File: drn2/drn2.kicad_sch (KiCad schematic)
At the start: 55 parts, among them J1 Conn_01x03_Socket, J10 Conn_01x03_Socket, J11 Conn_01x03_Socket, J12 Conn_01x03_Socket, J13 Conn_01x03_Socket, J14GND Conn_01x03_Socket, J15GND Conn_01x03_Socket, J16 Conn_01x03_Socket, J2 Raspberry_Pi_2_3, J3 Conn_01x03_Socket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

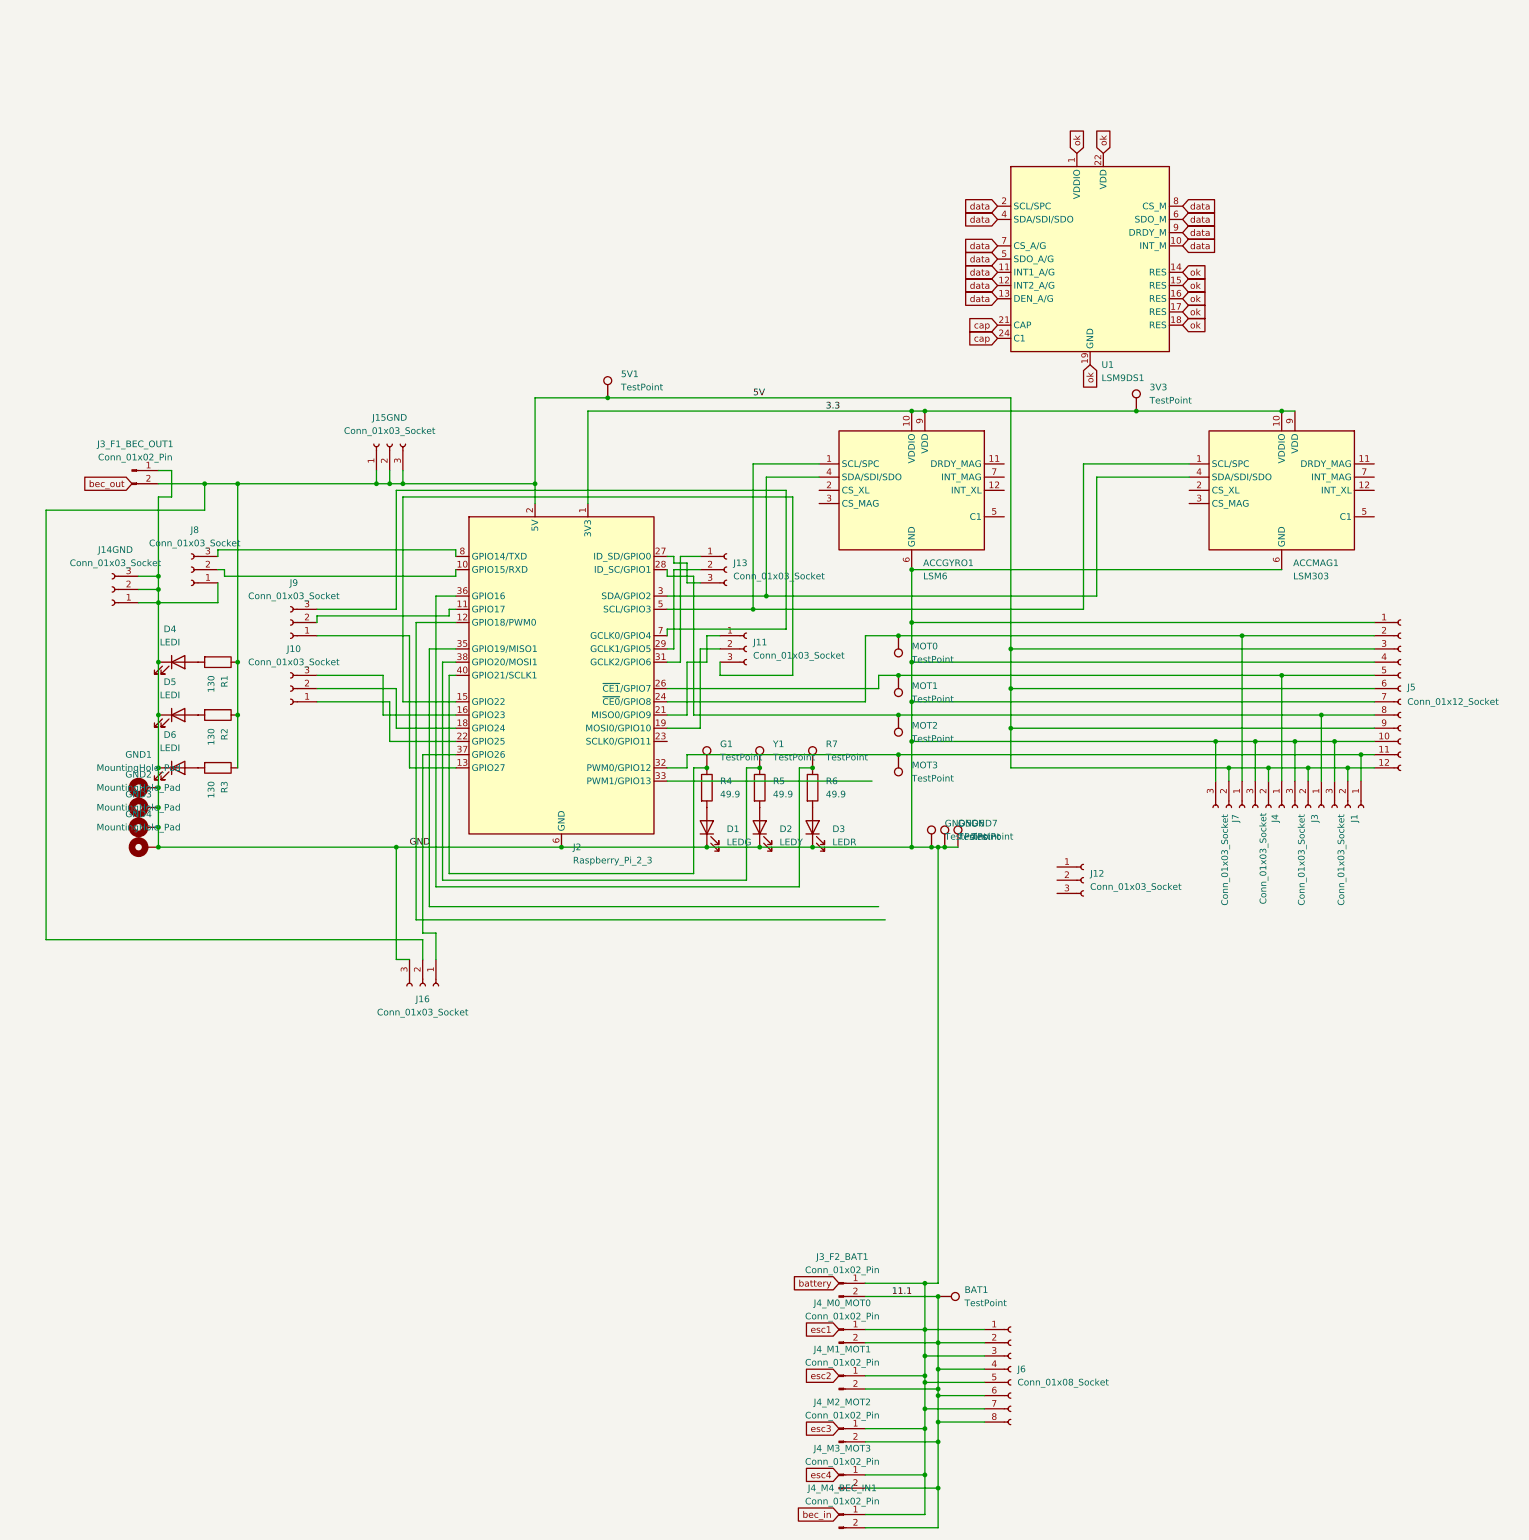
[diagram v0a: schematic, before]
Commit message: feat: pcb version 2.8
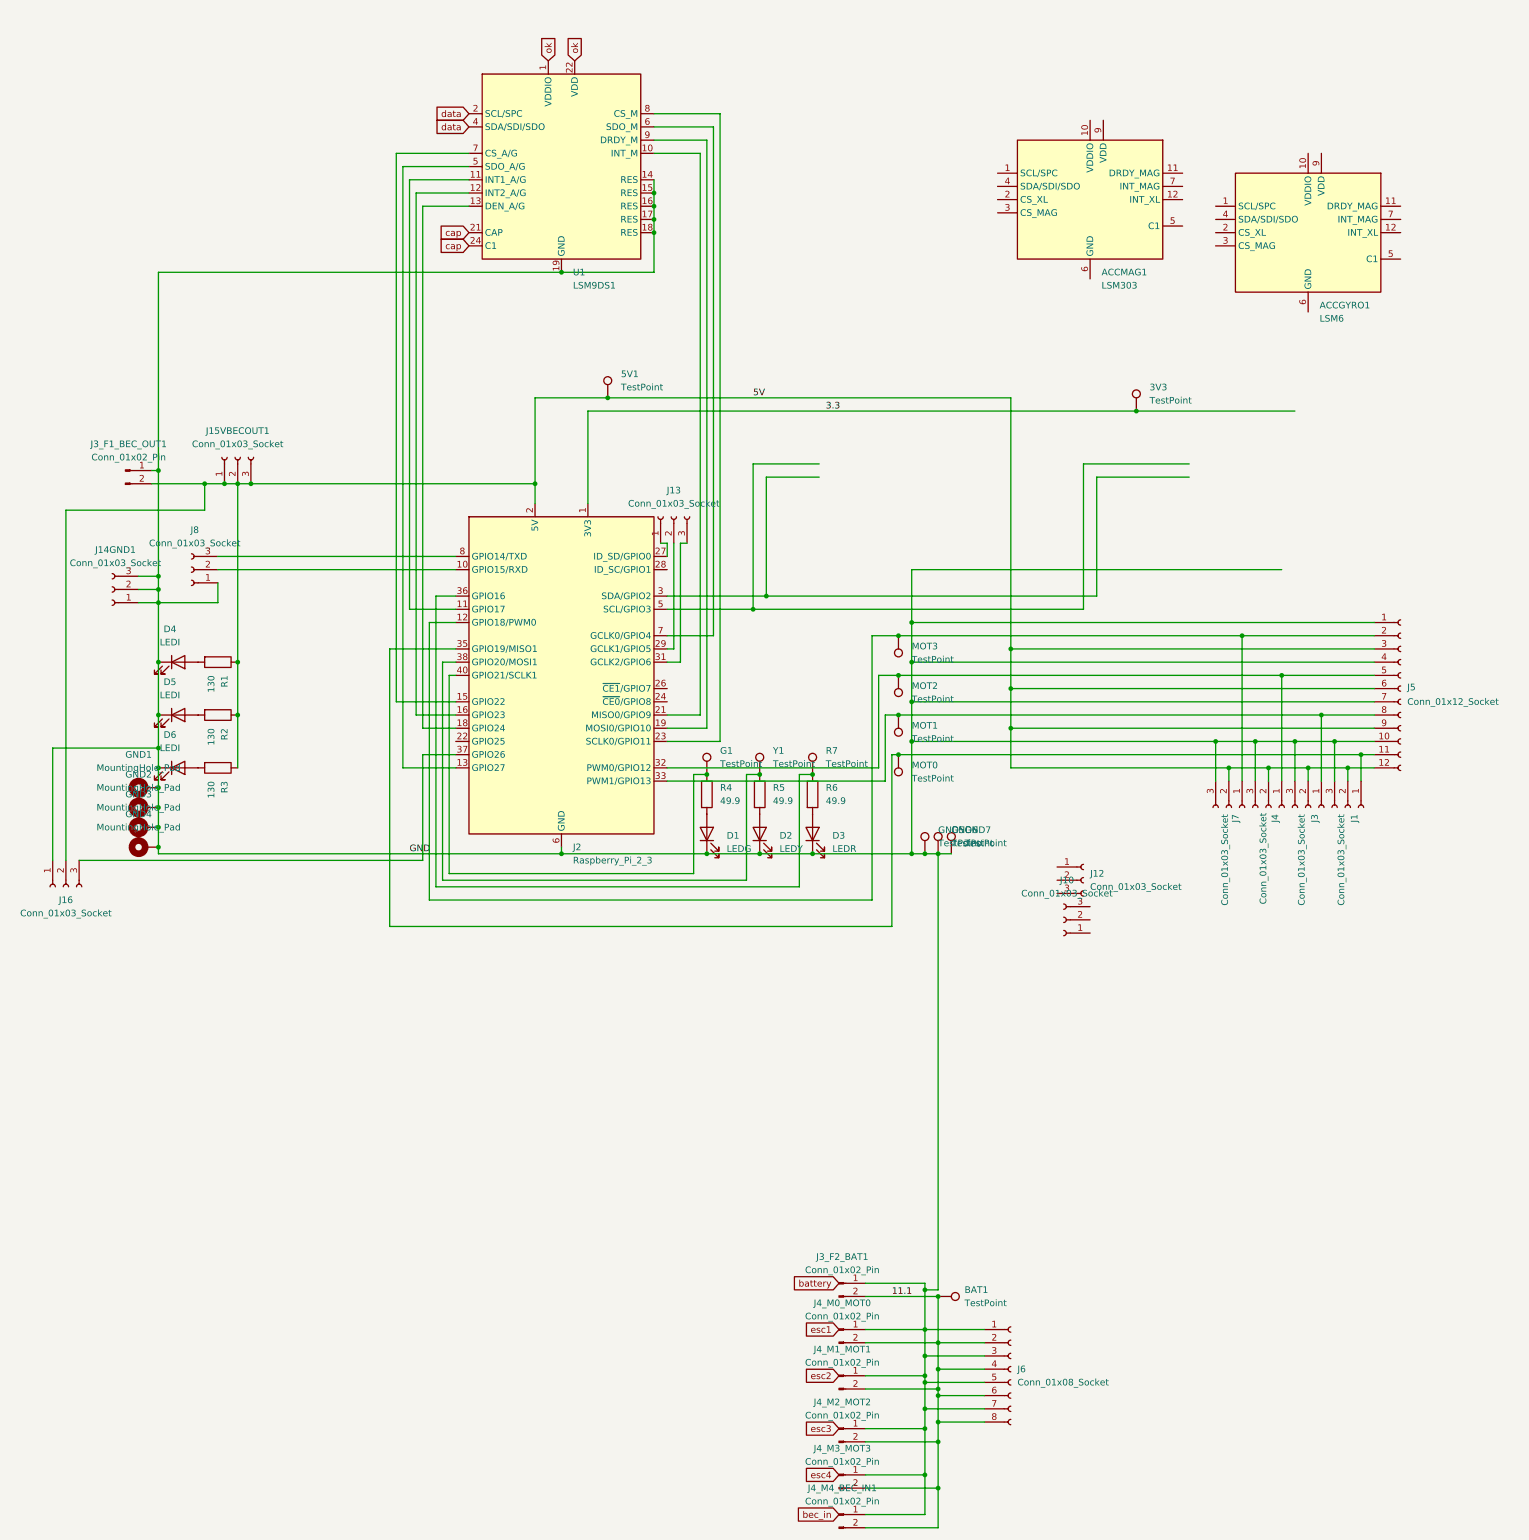
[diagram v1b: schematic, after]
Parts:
- removed J11, J9: Conn_01x03_Socket, Connector_PinHeader_2.54mm:PinHeader_1x03_P2.54mm_Vertical, symbol Connector:Conn_01x03_Socket
- ACCGYRO1, ACCMAG1, J5, J8: JLCPCB BOM (none) -> 0
- renumbered J14GND to J14GND1, J15GND to J15VBECOUT1, MOT3 to MOT0, MOT2 to MOT1, MOT1 to MOT2, MOT0 to MOT3
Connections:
- net 3.3: no longer ACCGYRO1.10 (VDDIO), ACCGYRO1.9 (VDD), ACCMAG1.10 (VDDIO), ACCMAG1.9 (VDD)
- net GND: now also J16.1 (Pin_1), U1.14 (RES), U1.15 (RES), U1.16 (RES), U1.17 (RES), U1.18 (RES), U1.19 (GND), U1.20 (GND); no longer ACCGYRO1.6 (GND), ACCGYRO1.8 (GND), ACCMAG1.6 (GND), ACCMAG1.8 (GND), J16.3 (Pin_3)
- net data: no longer U1.10 (INT_M), U1.11 (INT1_A/G), U1.12 (INT2_A/G), U1.13 (DEN_A/G), U1.5 (SDO_A/G), U1.6 (SDO_M), U1.7 (CS_A/G), U1.8 (CS_M), U1.9 (DRDY_M)
- net ok: no longer U1.14 (RES), U1.15 (RES), U1.16 (RES), U1.17 (RES), U1.18 (RES), U1.19 (GND), U1.20 (GND)
- net at J1.1 (Pin_1), J5.11 (Pin_11), MOT0.1: now also J2.35 (GPIO19/MISO1); no longer J2.32 (PWM0/GPIO12)
- net at J5.2 (Pin_2), J7.1 (Pin_1), MOT3.1: now also J2.12 (GPIO18/PWM0); no longer J2.24 (~{CE0}/GPIO8)
- net at J4.1 (Pin_1), J5.5 (Pin_5), MOT2.1: now also J2.32 (PWM0/GPIO12); no longer J2.26 (~{CE1}/GPIO7)
- net at J3.1 (Pin_1), J5.8 (Pin_8), MOT1.1: now also J2.33 (PWM1/GPIO13); no longer J2.28 (ID_SC/GPIO1)
- net at J2.37 (GPIO26): now also J16.3 (Pin_3); no longer J16.1 (Pin_1)
- net at J10.1 (Pin_1): no longer J2.22 (GPIO25)
- net at J10.2 (Pin_2): no longer J2.18 (GPIO24)
- net at J10.3 (Pin_3): no longer J2.16 (GPIO23)
- net at J2.13 (GPIO27): now also U1.5 (SDO_A/G)
- net at J2.11 (GPIO17): now also U1.11 (INT1_A/G)
- net at J2.7 (GCLK0/GPIO4): now also U1.6 (SDO_M)
- net at J2.15 (GPIO22): now also U1.7 (CS_A/G)
- net at J2.19 (MOSI0/GPIO10): now also U1.9 (DRDY_M)
- net at J2.21 (MISO0/GPIO9): now also U1.10 (INT_M)
- net at J2.23 (SCLK0/GPIO11): now also U1.8 (CS_M)
- net at J2.27 (ID_SD/GPIO0): now also J13.1 (Pin_1); no longer J13.3 (Pin_3)
- net at J2.31 (GCLK2/GPIO6): now also J13.3 (Pin_3); no longer J13.1 (Pin_1)
- new net: ACCGYRO1.6 (GND), ACCGYRO1.8 (GND)
- new net: ACCMAG1.6 (GND), ACCMAG1.8 (GND)
- new net: J2.16 (GPIO23), U1.12 (INT2_A/G)
- new net: J2.18 (GPIO24), U1.13 (DEN_A/G)
- now unconnected: ACCGYRO1.1 (SCL/SPC), ACCGYRO1.4 (SDA/SDI/SDO), ACCMAG1.1 (SCL/SPC), ACCMAG1.4 (SDA/SDI/SDO), J2.3 (SDA/GPIO2), J2.5 (SCL/GPIO3)
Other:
- moved on the sheet: D1, D2, D3, G1, GND5, GND6, GND7, J10, J13, J15VBECOUT1, J16, J3_F1_BEC_OUT1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

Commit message: feat: pcb v3
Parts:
- removed 3V3: TestPoint, TestPoint:TestPoint_Pad_D1.0mm, symbol Connector:TestPoint
- removed ACCGYRO1: LSM6, Package_LGA:LGA-12_2x2mm_P0.5mm, symbol Sensor_Motion:LSM303C
- removed ACCMAG1: LSM303, Package_LGA:LGA-12_2x2mm_P0.5mm, symbol Sensor_Motion:LSM303C
- removed J10: Conn_01x03_Socket, Connector_PinHeader_2.54mm:PinHeader_1x03_P2.54mm_Vertical, symbol Connector:Conn_01x03_Socket
- added C1, C2, C3: 100nF, Capacitor_SMD:C_0603_1608Metric_Pad1.08x0.95mm_HandSolder, symbol Device:C
- added C4: C_Polarized, Capacitor_SMD:CP_Elec_4x5.4, symbol Device:C_Polarized
- added C5: 10nF, Capacitor_SMD:C_0603_1608Metric_Pad1.08x0.95mm_HandSolder, symbol Device:C
- added R10, R11, R8, R9: 130, Resistor_SMD:R_0603_1608Metric, symbol Device:R
- added VDD1, VDDIO1: TestPoint, TestPoint:TestPoint_Pad_D1.0mm, symbol Connector:TestPoint
- GND1, GND2, GND3, GND4: JLCPCB BOM (none) -> 0
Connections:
- net 5V: now also R10.2, R11.2; no longer J3_F1_BEC_OUT1.2 (Pin_2)
- net GND: now also J1.1 (Pin_1), J2.35 (GPIO19/MISO1), J5.11 (Pin_11), MOT0.1, C1.2, C2.1, C3.1, C4.2, C5.2, R8.1, R9.1
- net at J2.11 (GPIO17): now also U1.12 (INT2_A/G); no longer U1.11 (INT1_A/G)
- net at J2.13 (GPIO27): now also U1.11 (INT1_A/G); no longer U1.5 (SDO_A/G)
- net at J2.15 (GPIO22): now also U1.9 (DRDY_M); no longer U1.7 (CS_A/G)
- net at J2.16 (GPIO23): now also U1.10 (INT_M); no longer U1.12 (INT2_A/G)
- net at J2.18 (GPIO24): now also U1.8 (CS_M); no longer U1.13 (DEN_A/G)
- net at J2.19 (MOSI0/GPIO10): now also U1.7 (CS_A/G); no longer U1.9 (DRDY_M)
- net at J2.21 (MISO0/GPIO9): now also U1.6 (SDO_M); no longer U1.10 (INT_M)
- net at J2.23 (SCLK0/GPIO11): now also U1.5 (SDO_A/G); no longer U1.8 (CS_M)
- net at J2.24 (~{CE0}/GPIO8): now also J13.1 (Pin_1)
- net at J2.26 (~{CE1}/GPIO7): now also J13.2 (Pin_2)
- net at J2.27 (ID_SD/GPIO0): now also J13.3 (Pin_3); no longer J13.1 (Pin_1)
- net at J2.28 (ID_SC/GPIO1): now also J12.1 (Pin_1)
- net at J2.29 (GCLK1/GPIO5): now also J12.2 (Pin_2); no longer J13.2 (Pin_2)
- net at J2.3 (SDA/GPIO2): now also U1.4 (SDA/SDI/SDO)
- net at J2.31 (GCLK2/GPIO6): now also J12.3 (Pin_3); no longer J13.3 (Pin_3)
- net at J2.5 (SCL/GPIO3): now also U1.2 (SCL/SPC)
- net at J2.7 (GCLK0/GPIO4): now also U1.13 (DEN_A/G); no longer U1.6 (SDO_M)
- net 3.3: no longer names the net of J2.1 (3V3), J2.17 (3V3)
- net cap: no longer names the net of U1.21 (CAP)
- net cap: now also C5.1; no longer U1.24 (C1)
- removed net data: U1.2 (SCL/SPC), U1.4 (SDA/SDI/SDO)
- net ok: no longer names the net of U1.1 (VDDIO), U1.3 (VDDIO)
- net ok: now also C2.2, R11.1, R9.2, VDDIO1.1; no longer U1.22 (VDD), U1.23 (VDD)
- new net: C3.2, C4.1, R10.1, R8.2, U1.22 (VDD), U1.23 (VDD), VDD1.1
- new net: C1.1, U1.24 (C1)
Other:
- moved on the sheet: J12, J13

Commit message: feat: new pcb version, removed mess
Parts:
- C4: LCSC Part C213487 -> C72483
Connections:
- net 5V: now also J3_F1_BEC_OUT1.2 (Pin_2)
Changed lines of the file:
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@@
 	)
 	(junction
+		(at 48.26 60.96)
+		(diameter 0)
+		(color 0 0 0 0)
+	)
+	(junction
 		(at 154.94 116.84)
 		(diameter 0)
@@
 	(wire
 		(pts
+			(xy 38.1 60.96) (xy 48.26 60.96)
+		)
+		(stroke
+			(width 0)
+			(type default)
+		)
+	)
+	(wire
+		(pts
 			(xy 273.05 90.17) (xy 247.65 90.17)
 		)
@@
 			)
 		)
-		(property "LCSC Part" "C213487"
+		(property "LCSC Part" "C72483"
 			(at 48.26 24.13 0)
 			(effects

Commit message: feat: drn pcb v3 almost done
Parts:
- removed G1, GND5, GND6, R7, Y1: TestPoint, TestPoint:TestPoint_Pad_D1.0mm, symbol Connector:TestPoint
- removed J12, J13: Conn_01x03_Socket, Connector_PinHeader_2.54mm:PinHeader_1x03_P2.54mm_Vertical, symbol Connector:Conn_01x03_Socket
- removed J3_F1_BEC_OUT1, J4_M4_BEC_IN1: Conn_01x02_Pin, Connector_AMASS:AMASS_XT60-F_1x02_P7.20mm_Vertical, symbol Connector:Conn_01x02_Pin
- removed J5: Conn_01x12_Socket, Connector_JST:JST_XH_B12B-XH-AM_1x12_P2.50mm_Vertical, symbol Connector:Conn_01x12_Socket
- removed J6: Conn_01x08_Socket, Connector_PinHeader_2.54mm:PinHeader_1x08_P2.54mm_Vertical, symbol Connector:Conn_01x08_Socket
- added D7: LEDI, LED_SMD:LED_0603_1608Metric, symbol Device:LED
- added J10: Conn_01x09_Socket, Connector_PinHeader_2.54mm:PinHeader_1x09_P2.54mm_Vertical, symbol Connector:Conn_01x09_Socket
- added J13: Conn_01x04_Socket, Connector_PinHeader_2.54mm:PinHeader_1x04_P2.54mm_Vertical, symbol Connector:Conn_01x04_Socket
- added J9: Conn_01x04_Pin, Connector_JST:JST_XH_B4B-XH-A_1x04_P2.50mm_Vertical, symbol Connector:Conn_01x04_Pin
- added R14: 300K, Resistor_SMD:R_0603_1608Metric, symbol Device:R
- added R15: 100k, Resistor_SMD:R_0603_1608Metric, symbol Device:R
- added R7: 130, Resistor_SMD:R_0603_1608Metric, symbol Device:R
- added SCL1, SDA3: TestPoint, TestPoint:TestPoint_Pad_D1.0mm, symbol Connector:TestPoint
- added U3: MCP3004, Package_DIP:DIP-14_W7.62mm, symbol Analog_ADC:MCP3004
- renumbered MOT0 to MO0, MOT1 to MO1, MOT2 to MO2, MOT3 to MO3, J2 to RPI02, J8 to TXRX1
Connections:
- net 5V: now also J13.4 (Pin_4), R7.1, U3.13 (Vref), U3.14 (Vdd)
- net GND: now also J3.1 (Pin_1), J4.1 (Pin_1), J7.1 (Pin_1), D7.1 (K), J10.1 (Pin_1), J13.1 (Pin_1), J9.4 (Pin_4), R15.1, U3.12 (AGND), U3.2 (CH1), U3.7 (DGND); no longer J1.3 (Pin_3), J3.3 (Pin_3), J4.3 (Pin_3), J7.3 (Pin_3), MO0.1, RPI02.35 (GPIO19/MISO1)
- net at C2.2, R11.1, R9.2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: now also U3.4 (CH3)
- net at MO3.1, RPI02.12 (GPIO18/PWM0): now also J7.3 (Pin_3); no longer J7.1 (Pin_1)
- net at TXRX1.2 (Pin_2): now also RPI02.8 (GPIO14/TXD); no longer RPI02.10 (GPIO15/RXD)
- net at TXRX1.3 (Pin_3): now also RPI02.10 (GPIO15/RXD); no longer RPI02.8 (GPIO14/TXD)
- net at MO2.1, RPI02.32 (PWM0/GPIO12): now also J4.3 (Pin_3); no longer J4.1 (Pin_1)
- net at MO1.1, RPI02.33 (PWM1/GPIO13): now also J3.3 (Pin_3); no longer J3.1 (Pin_1)
- net at C3.2, C4.1, R10.1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: now also U3.3 (CH2)
- net at RPI02.15 (GPIO22): now also U1.10 (INT_M); no longer U1.9 (DRDY_M)
- net at RPI02.16 (GPIO23): now also U1.9 (DRDY_M); no longer U1.10 (INT_M)
- net at RPI02.19 (MOSI0/GPIO10): now also U3.9 (Din); no longer U1.7 (CS_A/G)
- net at RPI02.21 (MISO0/GPIO9): now also U3.10 (Dout); no longer U1.6 (SDO_M)
- net at RPI02.23 (SCLK0/GPIO11): now also U3.11 (CLK); no longer U1.5 (SDO_A/G)
- net at RPI02.24 (~{CE0}/GPIO8): now also U3.8 (~{CS}/SHDN)
- net at RPI02.26 (~{CE1}/GPIO7): now also U1.7 (CS_A/G)
- net at RPI02.27 (ID_SD/GPIO0): now also U1.6 (SDO_M)
- net at RPI02.28 (ID_SC/GPIO1): now also U1.5 (SDO_A/G)
- net at RPI02.29 (GCLK1/GPIO5): now also J13.2 (Pin_2)
- net at RPI02.3 (SDA/GPIO2), U1.4 (SDA/SDI/SDO): now also SDA3.1
- net at RPI02.31 (GCLK2/GPIO6): now also J13.3 (Pin_3)
- net at RPI02.5 (SCL/GPIO3), U1.2 (SCL/SPC): now also SCL1.1
- new net: J10.4 (Pin_4), J9.1 (Pin_1), R14.2
- new net: J10.3 (Pin_3), J9.2 (Pin_2)
- new net: J10.2 (Pin_2), J9.3 (Pin_3)
- new net: J1.3 (Pin_3), MO0.1, RPI02.35 (GPIO19/MISO1)
- new net: D7.2 (A), R7.2
- new net: R14.1, R15.2, U3.1 (CH0)
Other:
- moved on the sheet: J1, J3, J4, J7, TXRX1, VDD1

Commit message: drn v4
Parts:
- removed J10: Conn_01x09_Socket, Connector_PinHeader_2.54mm:PinHeader_1x09_P2.54mm_Vertical, symbol Connector:Conn_01x09_Socket
- removed TXRX1: Conn_01x03_Socket, Connector_PinHeader_2.54mm:PinHeader_1x03_P2.54mm_Vertical, symbol Connector:Conn_01x03_Socket
- removed U3: MCP3004, Package_DIP:DIP-14_W7.62mm, symbol Analog_ADC:MCP3004
- added I2C1, SPI1, UART1: Conn_01x04_Socket, Connector_PinHeader_2.54mm:PinHeader_1x04_P2.54mm_Vertical, symbol Connector:Conn_01x04_Socket
- added J2: Conn_01x04_Socket, Connector_PinSocket_2.54mm:PinSocket_1x04_P2.54mm_Vertical, symbol Connector:Conn_01x04_Socket
- added MAN1: ADS1115IDGS, Package_SO:TSSOP-10_3x3mm_P0.5mm, symbol Analog_ADC:ADS1115IDGS
- IMU1: renamed from U1; LCSC Part (none) -> C2655096
- J9: LCSC Part (none) -> C18077835
- R14: value 300K -> 7K5; LCSC Part (none) -> C728597
- R15: value 100k -> 2K5; LCSC Part (none) -> C304065
- TOF1: renamed from J13; JLCPCB BOM (none) -> 0
- renumbered J15VBECOUT1 to 5V1, 5V1 to 5V2, J14GND1 to GND1, GND1 to GND5, J16 to J37, RPI02 to RPI2
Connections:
- net 5V: now also I2C1.4 (Pin_4), MAN1.8 (VDD), SPI1.4 (Pin_4), UART1.4 (Pin_4)
- net GND: now also C1.1, C5.1, I2C1.1 (Pin_1), J2.1 (Pin_1), MAN1.3 (GND), SPI1.1 (Pin_1), UART1.1 (Pin_1); no longer C1.2, C5.2
- net at J9.1 (Pin_1), R14.2: now also J2.4 (Pin_4)
- net at J9.2 (Pin_2): now also J2.3 (Pin_3)
- net at J9.3 (Pin_3): now also J2.2 (Pin_2)
- net at IMU1.21 (CAP): now also C5.2; no longer C5.1
- net at IMU1.4 (SDA/SDI/SDO), RPI2.3 (SDA/GPIO2), SDA3.1: now also I2C1.3 (Pin_3), MAN1.9 (SDA)
- net at C2.2, IMU1.1 (VDDIO), IMU1.3 (VDDIO)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: now also MAN1.7 (AIN3)
- net at IMU1.2 (SCL/SPC), RPI2.5 (SCL/GPIO3), SCL1.1: now also I2C1.2 (Pin_2), MAN1.10 (SCL)
- net at RPI2.8 (GPIO14/TXD): now also UART1.2 (Pin_2)
- net at RPI2.10 (GPIO15/RXD): now also UART1.3 (Pin_3)
- net at R14.1, R15.2: now also MAN1.5 (AIN1)
- net at C3.2, C4.1, IMU1.22 (VDD)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: now also MAN1.6 (AIN2)
- net at RPI2.21 (MISO0/GPIO9): now also SPI1.3 (Pin_3)
- net at RPI2.23 (SCLK0/GPIO11): now also MAN1.2 (ALERT/RDY)
- net at RPI2.24 (~{CE0}/GPIO8): now also MAN1.1 (ADDR)
- net at RPI2.19 (MOSI0/GPIO10): now also SPI1.2 (Pin_2)
- net at RPI2.1 (3V3), RPI2.17 (3V3): now also MAN1.4 (AIN0)
- net at IMU1.24 (C1): now also C1.2; no longer C1.1
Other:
- moved on the sheet: C1, C5

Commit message: v4 done, requires FP check
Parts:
- 5V1, GND1, J37: LCSC Part C49257 -> C541850
- I2C1, SPI1, UART1: JLCPCB BOM 0 -> 1; LCSC Part (none) -> C2718488
- J2: LCSC Part (none) -> C2718488
- MAN1: LCSC Part (none) -> C37593
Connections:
- net at SPI1.2 (Pin_2): now also RPI2.21 (MISO0/GPIO9); no longer RPI2.19 (MOSI0/GPIO10)
- net at SPI1.3 (Pin_3): now also RPI2.19 (MOSI0/GPIO10); no longer RPI2.21 (MISO0/GPIO9)
- net at TOF1.2 (Pin_2): now also RPI2.31 (GCLK2/GPIO6); no longer RPI2.29 (GCLK1/GPIO5)
- net at TOF1.3 (Pin_3): now also RPI2.29 (GCLK1/GPIO5); no longer RPI2.31 (GCLK2/GPIO6)
- net at RPI2.15 (GPIO22): now also IMU1.9 (DRDY_M); no longer IMU1.10 (INT_M)
- net at RPI2.16 (GPIO23): now also IMU1.10 (INT_M); no longer IMU1.9 (DRDY_M)
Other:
- moved on the sheet: TOF1
